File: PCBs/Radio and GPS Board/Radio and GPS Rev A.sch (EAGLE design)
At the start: 7 parts

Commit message: So. many. changes.
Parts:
- removed PINAV: PINAVL1, pinavl1:PINAVL1
- removed U$3: PC104_BOARD, PC104 Board:PC104_BOARD
- added PINAV_CONNECTOR: HLE-110-02-X-DV-BE-A, HLE-110-02-X-DV-BE-A:HLE-110-02-X-DV-BE-A
- added U$1: PC104_NO_DIMENSION, Cubesat:PC104_NO_DIMENSION
- LITHIUM: value CUBESAT_LITHIUM -> LI-1; device Radio Board Rev B:CUBESAT_LITHIUM -> Cubesat:LI-1
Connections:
- net 3V3: now also U$1.3V3BUS1; no longer U$3.3V3BUS1
- net GND: now also PINAV_CONNECTOR.15, PINAV_CONNECTOR.7, U$1.GND1, U$1.GND10, U$1.GND2, U$1.GND3, U$1.GND4, U$1.GND5, U$1.GND6, U$1.GND7, U$1.GND8, U$1.GND9; no longer PINAV.GND, PINAV.GND2, U$3.GND1, U$3.GND10, U$3.GND2, U$3.GND3, U$3.GND4, U$3.GND5, U$3.GND6, U$3.GND7, U$3.GND8, U$3.GND9
- net GPS_PF: now also PINAV_CONNECTOR.6, U$1.GPS_PF; no longer PINAV.PF, U$3.GPS_PF
- net GPS_RX: now also PINAV_CONNECTOR.2, U$1.GPS_RX; no longer PINAV.RX, U$3.GPS_RX
- net GPS_TX: now also PINAV_CONNECTOR.1, U$1.GPS_TX; no longer PINAV.TXD0, U$3.GPS_TX
- net GPS_VPP: now also PINAV_CONNECTOR.5, U$1.GPS_VPP; no longer PINAV.VPP, U$3.GPS_VPP
- net LI_RX: now also U$1.LI_RX; no longer U$3.LI_RX
- net LI_TX: now also U$1.LI_TX; no longer U$3.LI_TX
- net OA_RESET: now also U$1.LI_OA_RST; no longer U$3.LI_OA_RST
- net SW3: now also U$1.SW3_BAT; no longer U$3.SW3_BAT
- net SW9: now also PINAV_CONNECTOR.14, PINAV_CONNECTOR.8, U$1.SW9_3V3; no longer PINAV.VDD, PINAV.VDD2, U$3.SW9_3V3
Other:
- moved on the sheet: C1, C2, C3, C4

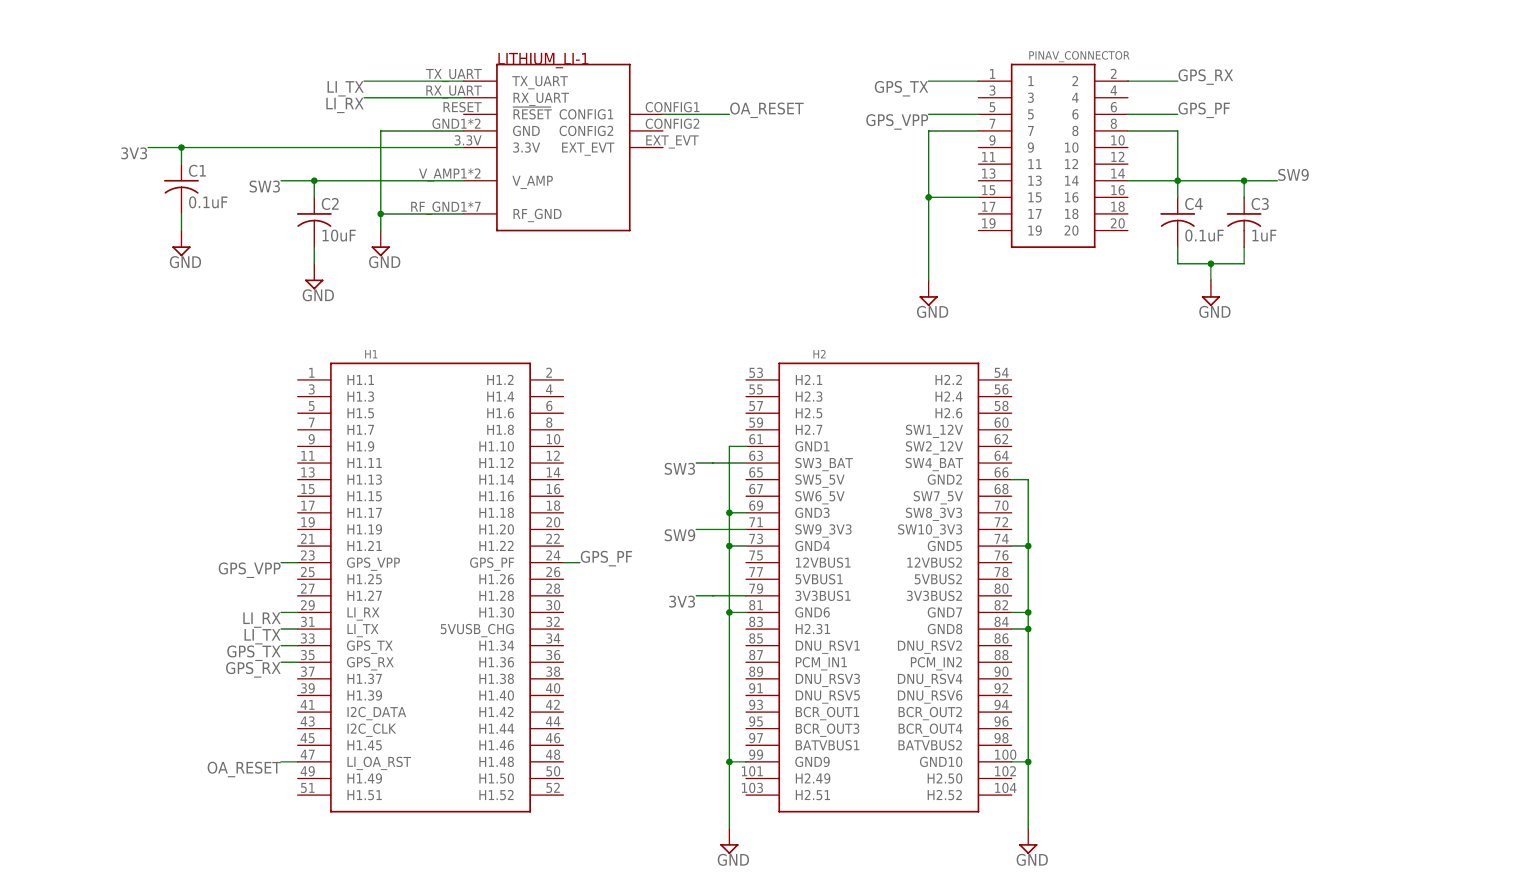
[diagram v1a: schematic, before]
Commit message: Add testpads, improve bypassing, update routing
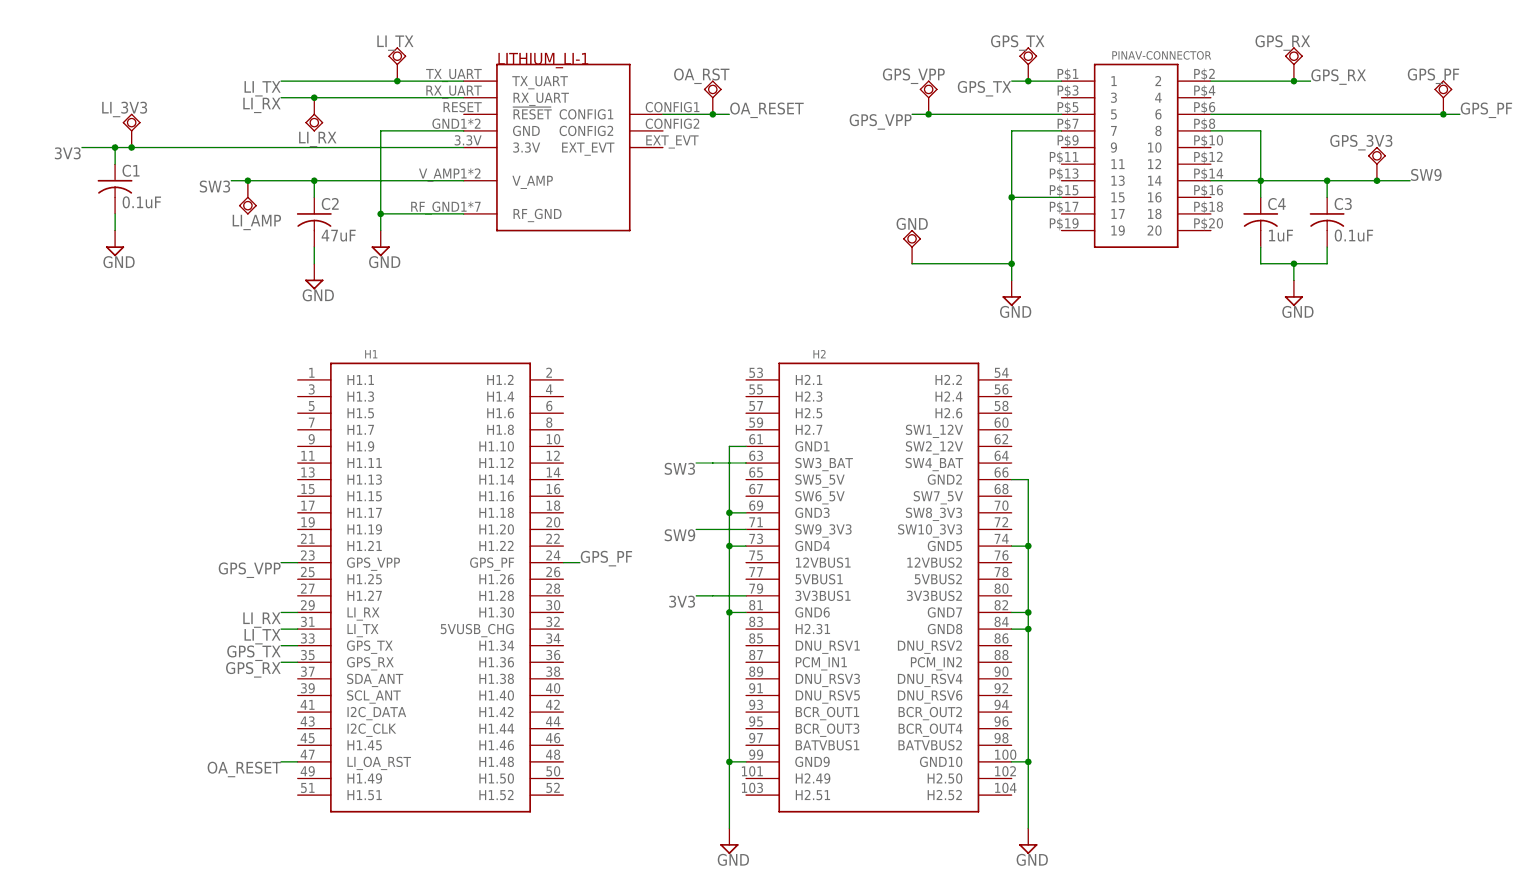
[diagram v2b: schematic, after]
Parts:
- removed PINAV_CONNECTOR: HLE-110-02-X-DV-BE-A, HLE-110-02-X-DV-BE-A:HLE-110-02-X-DV-BE-A
- added GND, GPS_3V3, GPS_PF, GPS_RX, GPS_TX, GPS_VPP, LI_3V3, LI_AMP, LI_RX, LI_TX, OA_RST: TPSQTP10SQ, testpad:TPSQTP10SQ
- added PINAV-CONNECTOR: HLE-110-02-X-DVHLE-110-X-DV-PE-BA, HLE-110-02-X-DV:HLE-110-02-X-DVHLE-110-X-DV-PE-BA
- C2: value 10uF -> 47uF
- C3: value 1uF -> 0.1uF
- C4: value 0.1uF -> 1uF
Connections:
- net 3V3: now also LI_3V3.TP
- net GND: now also GND.TP, PINAV-CONNECTOR.15, PINAV-CONNECTOR.7; no longer PINAV_CONNECTOR.15, PINAV_CONNECTOR.7
- net GPS_PF: now also GPS_PF.TP, PINAV-CONNECTOR.6; no longer PINAV_CONNECTOR.6
- net GPS_RX: now also GPS_RX.TP, PINAV-CONNECTOR.2; no longer PINAV_CONNECTOR.2
- net GPS_TX: now also GPS_TX.TP, PINAV-CONNECTOR.1; no longer PINAV_CONNECTOR.1
- net GPS_VPP: now also GPS_VPP.TP, PINAV-CONNECTOR.5; no longer PINAV_CONNECTOR.5
- net LI_RX: now also LI_RX.TP
- net LI_TX: now also LI_TX.TP
- net OA_RESET: now also OA_RST.TP
- net SW3: now also LI_AMP.TP
- net SW9: now also GPS_3V3.TP, PINAV-CONNECTOR.14, PINAV-CONNECTOR.8; no longer PINAV_CONNECTOR.14, PINAV_CONNECTOR.8
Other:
- moved on the sheet: C1, C3, C4

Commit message: Replace radio with Li-2 footprint
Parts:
- removed LITHIUM: LI-1, Cubesat:LI-1
- added LITHIUM-2: LI-2, Cubesat:LI-2
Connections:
- net 3V3: now also LITHIUM-2.3.3V; no longer LITHIUM.3.3V
- net GND: now also LITHIUM-2.GND, LITHIUM-2.RF_GND; no longer LITHIUM.GND, LITHIUM.RF_GND
- net LI_RX: now also LITHIUM-2.RX_UART; no longer LITHIUM.RX_UART
- net LI_TX: now also LITHIUM-2.TX_UART; no longer LITHIUM.TX_UART
- net OA_RESET: now also LITHIUM-2.CONFIG1; no longer LITHIUM.CONFIG1
- net SW3: now also LITHIUM-2.V_AMP; no longer LITHIUM.V_AMP
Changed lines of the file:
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@@
 <part name="C3" library="resistor" library_urn="urn:adsk.eagle:library:348" deviceset="C-US" device="C0805" package3d_urn="urn:adsk.eagle:package:23617/2" value="0.1uF"/>
 <part name="C4" library="resistor" library_urn="urn:adsk.eagle:library:348" deviceset="C-US" device="C0805" package3d_urn="urn:adsk.eagle:package:23617/2" value="1uF"/>
-<part name="LITHIUM" library="Cubesat" deviceset="LI-1" device=""/>
 <part name="SUPPLY8" library="supply2" library_urn="urn:adsk.eagle:library:372" deviceset="GND" device=""/>
 <part name="SUPPLY9" library="supply2" library_urn="urn:adsk.eagle:library:372" deviceset="GND" device=""/>
@@
 <part name="GPS_VPP" library="testpad" library_urn="urn:adsk.eagle:library:385" deviceset="TPSQ" device="TP10SQ" package3d_urn="urn:adsk.eagle:package:27962/1"/>
 <part name="GND" library="testpad" library_urn="urn:adsk.eagle:library:385" deviceset="TPSQ" device="TP10SQ" package3d_urn="urn:adsk.eagle:package:27962/1"/>
+<part name="LITHIUM-2" library="Cubesat" deviceset="LI-2" device=""/>
 </parts>
 <sheets>
@@
 <instance part="C3" gate="G$1" x="180.34" y="55.88"/>
 <instance part="C4" gate="G$1" x="170.18" y="55.88"/>
-<instance part="LITHIUM" gate="G$1" x="53.34" y="53.34"/>
 <instance part="SUPPLY8" gate="GND" x="175.26" y="43.18"/>
 <instance part="SUPPLY9" gate="GND" x="132.08" y="43.18"/>
@@
 <instance part="GPS_VPP" gate="G$1" x="119.38" y="73.66" rot="R180"/>
 <instance part="GND" gate="G$1" x="116.84" y="50.8" rot="R180"/>
+<instance part="LITHIUM-2" gate="G$1" x="53.34" y="53.34"/>
 </instances>
 <busses>
@@
 <wire x1="48.26" y1="76.2" x2="38.1" y2="76.2" width="0.1524" layer="91"/>
 <label x="20.32" y="76.2" size="1.778" layer="95" rot="R180"/>
-<pinref part="LITHIUM" gate="G$1" pin="TX_UART"/>
 <pinref part="LI_TX" gate="G$1" pin="TP"/>
 <wire x1="38.1" y1="76.2" x2="20.32" y2="76.2" width="0.1524" layer="91"/>
 <junction x="38.1" y="76.2"/>
+<pinref part="LITHIUM-2" gate="G$1" pin="TX_UART"/>
 </segment>
 <segment>
@@
 <wire x1="48.26" y1="73.66" x2="25.4" y2="73.66" width="0.1524" layer="91"/>
 <label x="20.32" y="73.66" size="1.778" layer="95" rot="R180"/>
-<pinref part="LITHIUM" gate="G$1" pin="RX_UART"/>
 <pinref part="LI_RX" gate="G$1" pin="TP"/>
 <wire x1="25.4" y1="73.66" x2="20.32" y2="73.66" width="0.1524" layer="91"/>
 <junction x="25.4" y="73.66"/>
+<pinref part="LITHIUM-2" gate="G$1" pin="RX_UART"/>
 </segment>
 <segment>
@@
 <wire x1="25.4" y1="58.42" x2="25.4" y2="60.96" width="0.1524" layer="91"/>
 <junction x="25.4" y="60.96"/>
-<pinref part="LITHIUM" gate="G$1" pin="V_AMP"/>
 <pinref part="LI_AMP" gate="G$1" pin="TP"/>
 <junction x="15.24" y="60.96"/>
+<pinref part="LITHIUM-2" gate="G$1" pin="V_AMP"/>
 </segment>
 <segment>
@@
 <net name="OA_RESET" class="0">
 <segment>
-<wire x1="78.74" y1="71.12" x2="86.36" y2="71.12" width="0.1524" layer="91"/>
+<wire x1="78.74" y1="71.12" x2="81.28" y2="71.12" width="0.1524" layer="91"/>
 <label x="88.9" y="71.12" size="1.778" layer="95"/>
-<pinref part="LITHIUM" gate="G$1" pin="CONFIG1"/>
 <pinref part="OA_RST" gate="G$1" pin="TP"/>
+<wire x1="81.28" y1="71.12" x2="86.36" y2="71.12" width="0.1524" layer="91"/>
 <wire x1="86.36" y1="71.12" x2="88.9" y2="71.12" width="0.1524" layer="91"/>
 <junction x="86.36" y="71.12"/>
+<pinref part="LITHIUM-2" gate="G$1" pin="CONFIG1"/>
+<junction x="81.28" y="71.12"/>
 </segment>
 <segment>
@@
 <wire x1="35.56" y1="55.88" x2="35.56" y2="53.34" width="0.1524" layer="91"/>
 <junction x="35.56" y="55.88"/>
-<pinref part="LITHIUM" gate="G$1" pin="GND"/>
-<pinref part="LITHIUM" gate="G$1" pin="RF_GND"/>
+<pinref part="LITHIUM-2" gate="G$1" pin="GND"/>
+<pinref part="LITHIUM-2" gate="G$1" pin="RF_GND"/>
 </segment>
 <segment>
@@
 <junction x="-5.08" y="66.04"/>
 <label x="-10.16" y="66.04" size="1.778" layer="95" rot="R180"/>
-<pinref part="LITHIUM" gate="G$1" pin="3.3V"/>
 <pinref part="LI_3V3" gate="G$1" pin="TP"/>
 <junction x="-2.54" y="66.04"/>
-</segment>
-<segment>
+<pinref part="LITHIUM-2" gate="G$1" pin="3.3V"/>
+</segment>
+<segment>

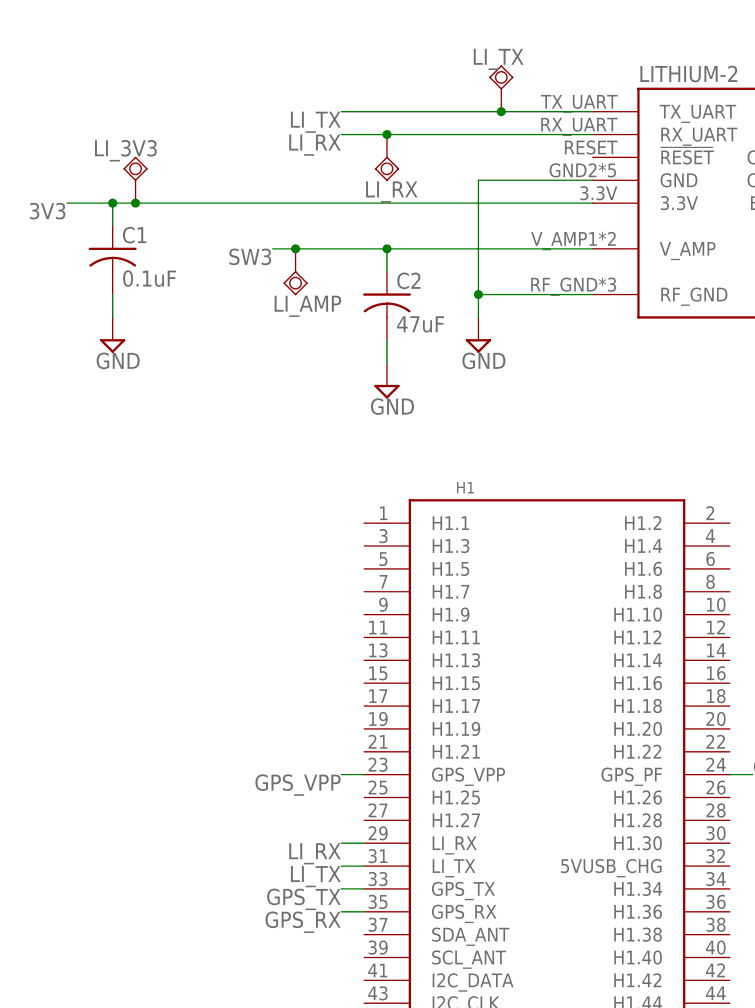
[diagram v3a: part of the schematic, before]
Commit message: Add Lithium reset pin
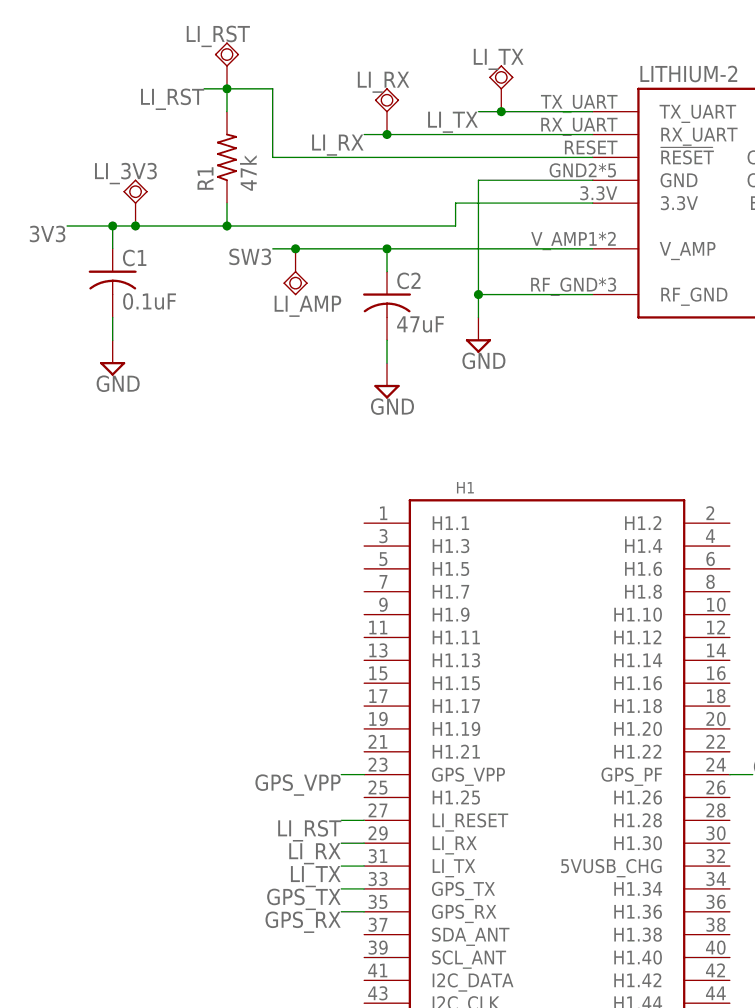
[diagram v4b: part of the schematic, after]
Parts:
- added LI_RST: TPSQTP10SQ, testpad:TPSQTP10SQ
- added R1: 47k, resistor:R-US_R0805
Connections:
- new net LI_RST: LITHIUM-2.!RESET, LI_RST.TP, R1.2, U$1.LI_RESET
- net 3V3: now also R1.1
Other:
- moved on the sheet: C1, LI_3V3, LI_RX
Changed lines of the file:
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@@
 <part name="GND" library="testpad" library_urn="urn:adsk.eagle:library:385" deviceset="TPSQ" device="TP10SQ" package3d_urn="urn:adsk.eagle:package:27962/1"/>
 <part name="LITHIUM-2" library="Cubesat" deviceset="LI-2" device=""/>
+<part name="LI_RST" library="testpad" library_urn="urn:adsk.eagle:library:385" deviceset="TPSQ" device="TP10SQ" package3d_urn="urn:adsk.eagle:package:27962/1"/>
+<part name="R1" library="resistor" library_urn="urn:adsk.eagle:library:348" deviceset="R-US_" device="R0805" package3d_urn="urn:adsk.eagle:package:23553/2" value="47k"/>
 </parts>
 <sheets>
@@
 </plain>
 <instances>
-<instance part="C1" gate="G$1" x="-5.08" y="60.96"/>
-<instance part="SUPPLY1" gate="GND" x="-5.08" y="50.8"/>
+<instance part="C1" gate="G$1" x="-5.08" y="58.42"/>
+<instance part="SUPPLY1" gate="GND" x="-5.08" y="48.26"/>
 <instance part="SUPPLY2" gate="GND" x="35.56" y="50.8"/>
 <instance part="SUPPLY5" gate="GND" x="88.9" y="-40.64"/>
@@
 <instance part="OA_RST" gate="G$1" x="86.36" y="73.66" rot="R180"/>
 <instance part="LI_TX" gate="G$1" x="38.1" y="78.74" rot="R180"/>
-<instance part="LI_RX" gate="G$1" x="25.4" y="71.12"/>
-<instance part="LI_3V3" gate="G$1" x="-2.54" y="68.58" rot="R180"/>
+<instance part="LI_RX" gate="G$1" x="25.4" y="76.2" rot="R180"/>
+<instance part="LI_3V3" gate="G$1" x="-2.54" y="66.04" rot="R180"/>
 <instance part="LI_AMP" gate="G$1" x="15.24" y="58.42"/>
 <instance part="GPS_3V3" gate="G$1" x="187.96" y="63.5" rot="R180"/>
@@
 <instance part="GND" gate="G$1" x="116.84" y="50.8" rot="R180"/>
 <instance part="LITHIUM-2" gate="G$1" x="53.34" y="53.34"/>
+<instance part="LI_RST" gate="G$1" x="7.62" y="81.28" rot="R180"/>
+<instance part="R1" gate="G$1" x="7.62" y="71.12" rot="R90"/>
 </instances>
 <busses>
@@
 <segment>
 <wire x1="48.26" y1="76.2" x2="38.1" y2="76.2" width="0.1524" layer="91"/>
-<label x="20.32" y="76.2" size="1.778" layer="95" rot="R180"/>
+<label x="35.56" y="76.2" size="1.778" layer="95" rot="R180"/>
 <pinref part="LI_TX" gate="G$1" pin="TP"/>
-<wire x1="38.1" y1="76.2" x2="20.32" y2="76.2" width="0.1524" layer="91"/>
+<wire x1="38.1" y1="76.2" x2="35.56" y2="76.2" width="0.1524" layer="91"/>
 <junction x="38.1" y="76.2"/>
 <pinref part="LITHIUM-2" gate="G$1" pin="TX_UART"/>
@@
 <segment>
 <wire x1="48.26" y1="73.66" x2="25.4" y2="73.66" width="0.1524" layer="91"/>
-<label x="20.32" y="73.66" size="1.778" layer="95" rot="R180"/>
+<label x="22.86" y="73.66" size="1.778" layer="95" rot="R180"/>
 <pinref part="LI_RX" gate="G$1" pin="TP"/>
-<wire x1="25.4" y1="73.66" x2="20.32" y2="73.66" width="0.1524" layer="91"/>
+<wire x1="25.4" y1="73.66" x2="22.86" y2="73.66" width="0.1524" layer="91"/>
 <junction x="25.4" y="73.66"/>
 <pinref part="LITHIUM-2" gate="G$1" pin="RX_UART"/>
@@
 <segment>
 <pinref part="C1" gate="G$1" pin="2"/>
-<wire x1="-5.08" y1="55.88" x2="-5.08" y2="53.34" width="0.1524" layer="91"/>
+<wire x1="-5.08" y1="53.34" x2="-5.08" y2="50.8" width="0.1524" layer="91"/>
 <pinref part="SUPPLY1" gate="GND" pin="GND"/>
 </segment>
@@
 <net name="3V3" class="0">
 <segment>
-<wire x1="48.26" y1="66.04" x2="-2.54" y2="66.04" width="0.1524" layer="91"/>
+<wire x1="48.26" y1="66.04" x2="33.02" y2="66.04" width="0.1524" layer="91"/>
 <pinref part="C1" gate="G$1" pin="1"/>
-<wire x1="-2.54" y1="66.04" x2="-5.08" y2="66.04" width="0.1524" layer="91"/>
-<wire x1="-5.08" y1="66.04" x2="-10.16" y2="66.04" width="0.1524" layer="91"/>
-<wire x1="-5.08" y1="66.04" x2="-5.08" y2="63.5" width="0.1524" layer="91"/>
-<junction x="-5.08" y="66.04"/>
-<label x="-10.16" y="66.04" size="1.778" layer="95" rot="R180"/>
+<wire x1="33.02" y1="66.04" x2="33.02" y2="63.5" width="0.1524" layer="91"/>
+<wire x1="33.02" y1="63.5" x2="7.62" y2="63.5" width="0.1524" layer="91"/>
+<wire x1="7.62" y1="63.5" x2="-2.54" y2="63.5" width="0.1524" layer="91"/>
+<wire x1="-2.54" y1="63.5" x2="-5.08" y2="63.5" width="0.1524" layer="91"/>
+<wire x1="-5.08" y1="63.5" x2="-10.16" y2="63.5" width="0.1524" layer="91"/>
+<wire x1="-5.08" y1="63.5" x2="-5.08" y2="60.96" width="0.1524" layer="91"/>
+<junction x="-5.08" y="63.5"/>
+<label x="-10.16" y="63.5" size="1.778" layer="95" rot="R180"/>
 <pinref part="LI_3V3" gate="G$1" pin="TP"/>
-<junction x="-2.54" y="66.04"/>
+<junction x="-2.54" y="63.5"/>
 <pinref part="LITHIUM-2" gate="G$1" pin="3.3V"/>
+<pinref part="R1" gate="G$1" pin="1"/>
+<wire x1="7.62" y1="66.04" x2="7.62" y2="63.5" width="0.1524" layer="91"/>
+<junction x="7.62" y="63.5"/>
 </segment>
 <segment>
@@
 </segment>
 </net>
+<net name="LI_RST" class="0">
+<segment>
+<pinref part="U$1" gate="A" pin="LI_RESET"/>
+<wire x1="22.86" y1="-2.54" x2="20.32" y2="-2.54" width="0.1524" layer="91"/>
+<label x="20.32" y="-2.54" size="1.778" layer="95" rot="R180"/>
+</segment>
+<segment>
+<pinref part="LITHIUM-2" gate="G$1" pin="!RESET"/>
+<wire x1="48.26" y1="71.12" x2="12.7" y2="71.12" width="0.1524" layer="91"/>
+<wire x1="12.7" y1="71.12" x2="12.7" y2="78.74" width="0.1524" layer="91"/>
+<wire x1="12.7" y1="78.74" x2="7.62" y2="78.74" width="0.1524" layer="91"/>
+<label x="5.08" y="78.74" size="1.778" layer="95" rot="R180"/>
+<pinref part="LI_RST" gate="G$1" pin="TP"/>
+<wire x1="7.62" y1="78.74" x2="5.08" y2="78.74" width="0.1524" layer="91"/>
+<junction x="7.62" y="78.74"/>
+<pinref part="R1" gate="G$1" pin="2"/>
+<wire x1="7.62" y1="76.2" x2="7.62" y2="78.74" width="0.1524" layer="91"/>
+</segment>
+</net>
